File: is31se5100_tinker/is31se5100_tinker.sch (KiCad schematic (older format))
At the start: 143 parts, among them J1 Screw_Terminal_01x02, J10 Conn_01x08, J11 Conn_01x08, J12 Conn_01x08, J13 Conn_01x08, J14 Conn_01x08, J15 Conn_01x08, J16 Conn_01x08, J17 Screw_Terminal_01x02, J18 Conn_01x08, J19 Conn_01x08, J2 USB_B_Micro, J20 Conn_01x08, J21 Screw_Terminal_01x02, J3 Conn_01x08, J4 Conn_01x08, J5 Conn_01x08, J6 Screw_Terminal_01x02, J7 Screw_Terminal_01x02, J8 Conn_01x08, J9 Conn_01x08, SW1 SW_SPDT, SW2 SW_SPDT, U1 Electrode, U10 Electrode, U100 Electrode, U101 Electrode, U102 Electrode, U103 Electrode, U104 Electrode, U105 Electrode, U106 Electrode, U107 Electrode, U108 Electrode, U109 Electrode, U11 Electrode, U110 Electrode, U111 Electrode, U112 Electrode, U113 Electrode, U114 Electrode, U115 Electrode, U116 Electrode, U117 Electrode, U118 Electrode, U119 Electrode, U12 Electrode, U120 Electrode, U13 Electrode, U14 Electrode, U15 Electrode, U16 Electrode, U17 Electrode, U18 Electrode, U19 Electrode, U2 Electrode, U20 Electrode, U21 Electrode, U22 Electrode, U23 Electrode, U24 Electrode, U25 Electrode, U26 Electrode, U27 Electrode, U28 Electrode, U29 Electrode, U3 Electrode, U30 Electrode, U31 Electrode, U32 Electrode, U33 Electrode, U34 Electrode, U35 Electrode, U36 Electrode, U37 Electrode, U38 Electrode, U39 Electrode, U4 Electrode, U40 Electrode, U41 Electrode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

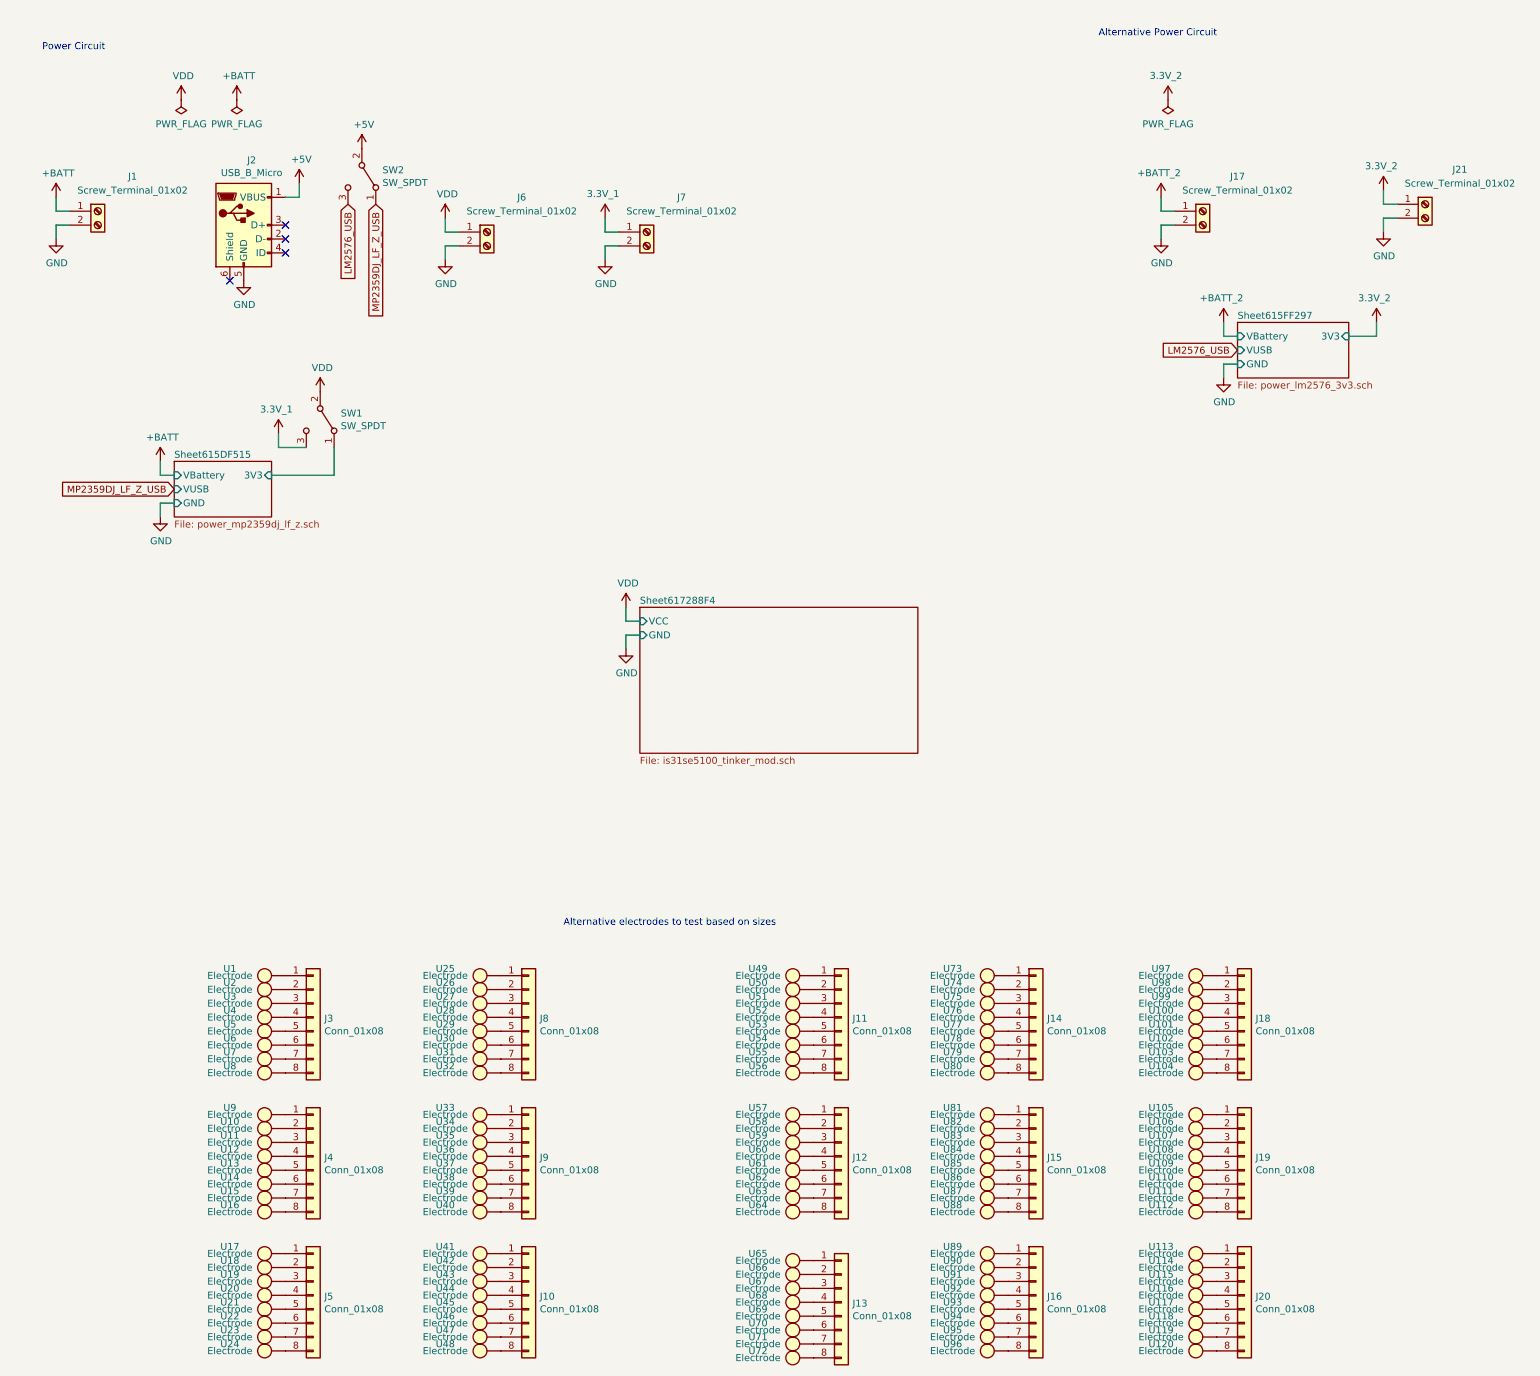
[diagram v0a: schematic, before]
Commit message: Established is31se5100_chained
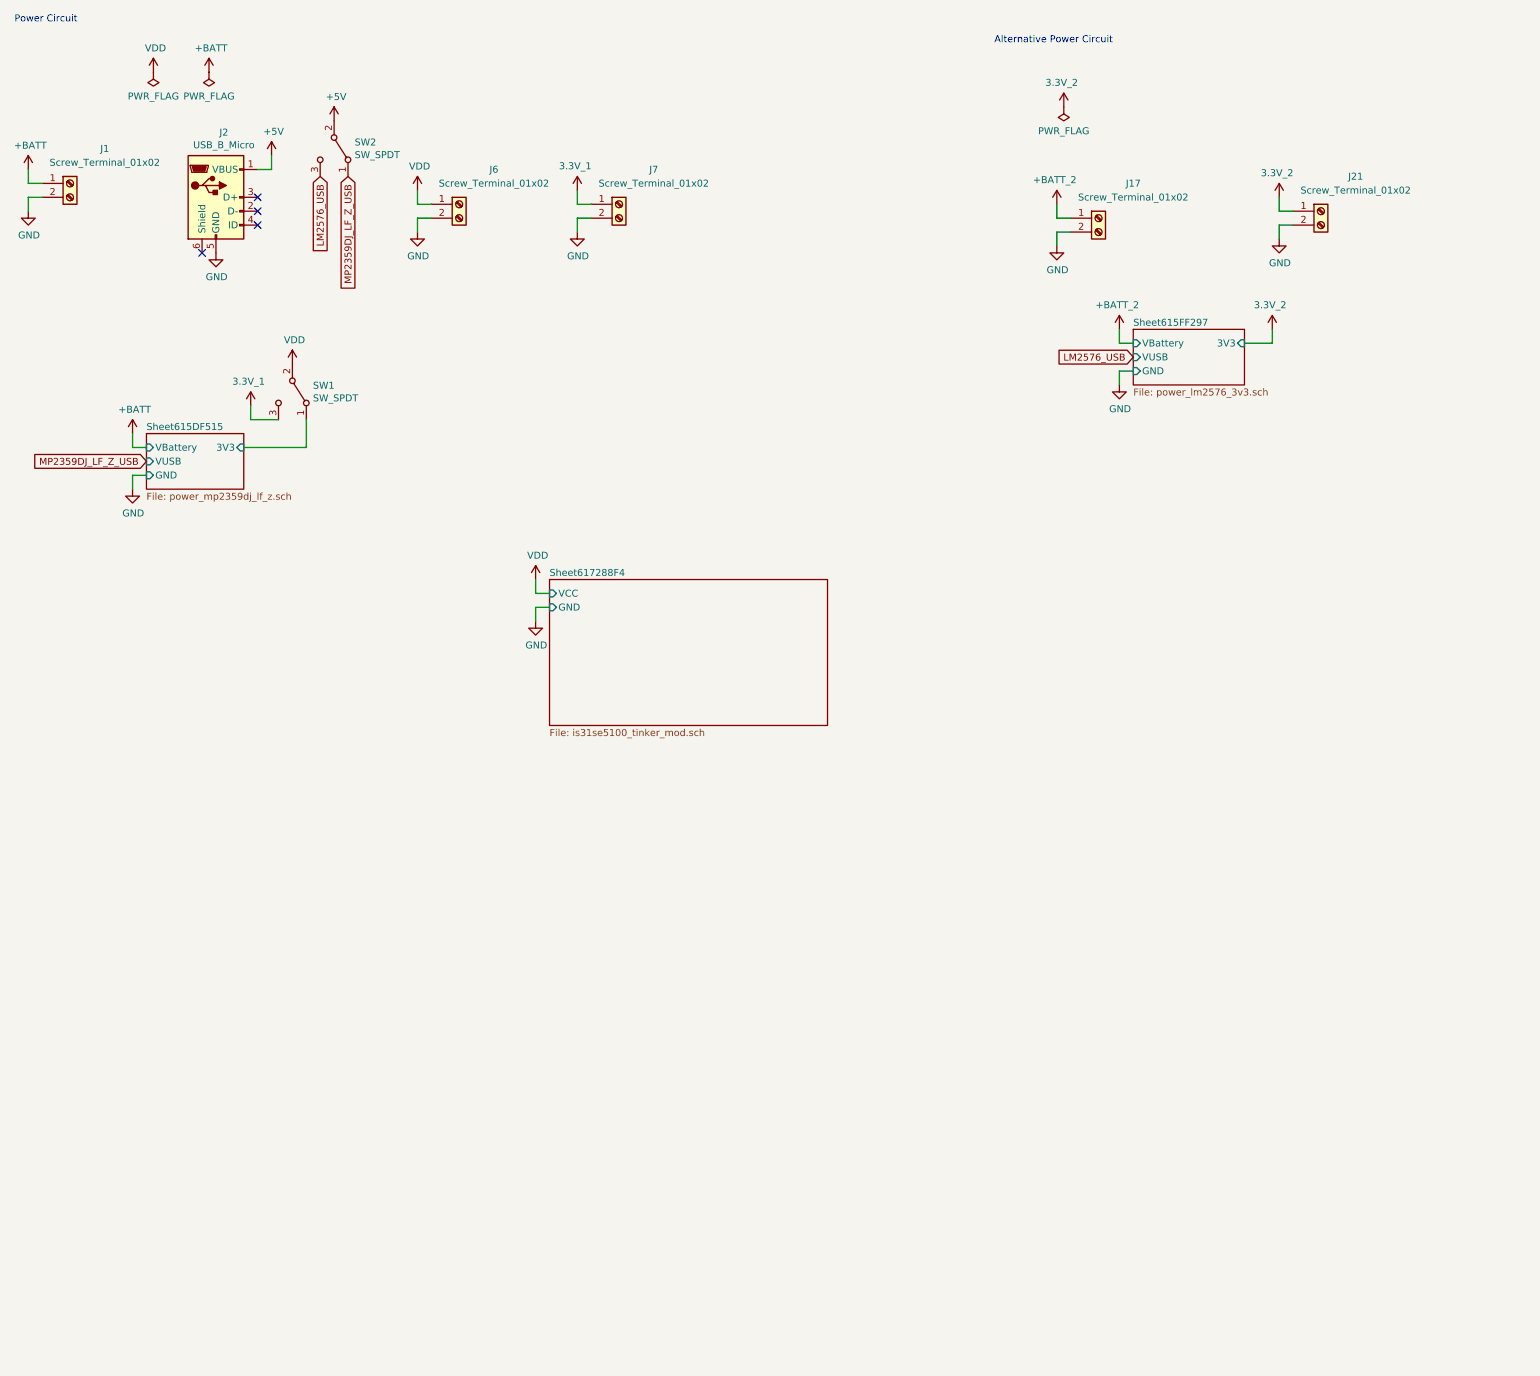
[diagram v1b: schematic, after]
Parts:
- removed J10, J11, J12, J13, J14, J15, J16, J18, J19, J20, J3, J4, J5, J8, J9: Conn_01x08, Connector_PinHeader_2.54mm:PinHeader_1x08_P2.54mm_Vertical, symbol Connector_Generic:Conn_01x08
- removed U1, U10, U100, U101, U102, U103, U104, U105, U106, U107, U108, U109, U11, U110, U111, U112, U113, U114, U115, U116, U117, U118, U119, U12, U120, U13, U14, U15, U16, U17, U18, U19, U2, U20, U21, U22, U23, U24, U25, U26, U27, U28, U29, U3, U30, U31, U32, U33, U34, U35, U36, U37, U38, U39, U4, U40, U41, U42, U43, U44, U45, U46, U47, U48, U49, U5, U50, U51, U52, U53, U54, U55, U56, U57, U58, U59, U6, U60, U61, U62, U63, U64, U65, U66, U67, U68, U69, U7, U70, U71, U72, U73, U74, U75, U76, U77, U78, U79, U8, U80, U81, U82, U83, U84, U85, U86, U87, U88, U89, U9, U90, U91, U92, U93, U94, U95, U96, U97, U98, U99: Electrode, symbol Custom_Sensor_Touch:Electrode
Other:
- note removed: "Alternative electrodes to test based on sizes"
- moved on the sheet: J1, J17, J2, J21, J6, J7, SW1, SW2
